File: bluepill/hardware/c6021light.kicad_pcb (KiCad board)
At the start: 2 copper layers, 100 x 50 mm, 82 parts, among them J1 Barrel_Jack_Switch, J10 Conn_01x02, J11 Conn_01x02, J12 XpressNet, J2 Conn_02x04_Odd_Even, J3 Conn_02x16_Row_Letter_First, J30 Loconet, J31 Conn_01x02, J32 Conn_01x02, J4 Conn_01x02, J5 Grove I2C, J50 USB_B_Micro, J51 Conn_01x06, J52 Debug UART, J6 Conn_01x02, J7 Conn_01x02, J8 RJ45, Q30 BC337, Q31 BC547, Q32 BC547, SW1 SW_Push, U1 L7805, U10 SN75176, U2 L7808, U3 MCP2562, U30 LM393, U4 ISO1050DUB, U50 CH340C

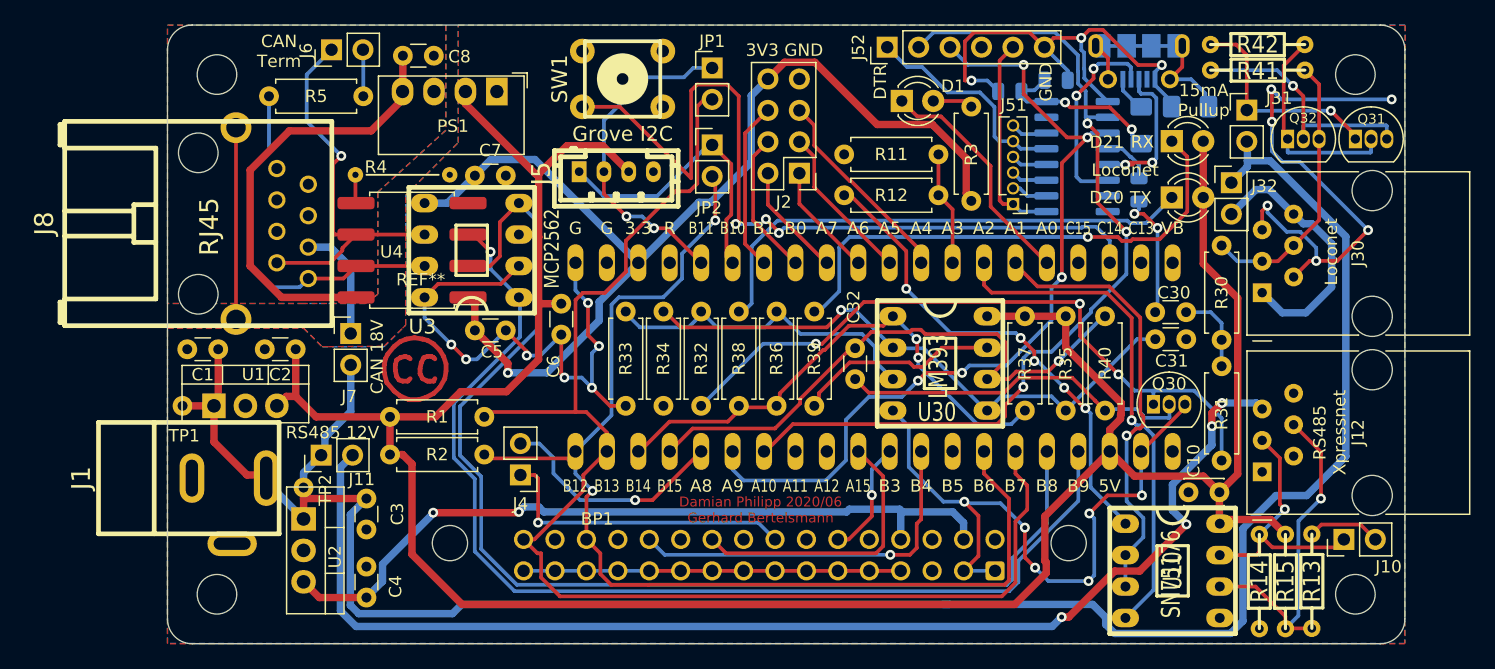
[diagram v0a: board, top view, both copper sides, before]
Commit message: new PCB version 1.1. aka 2020/08 with some small fixes
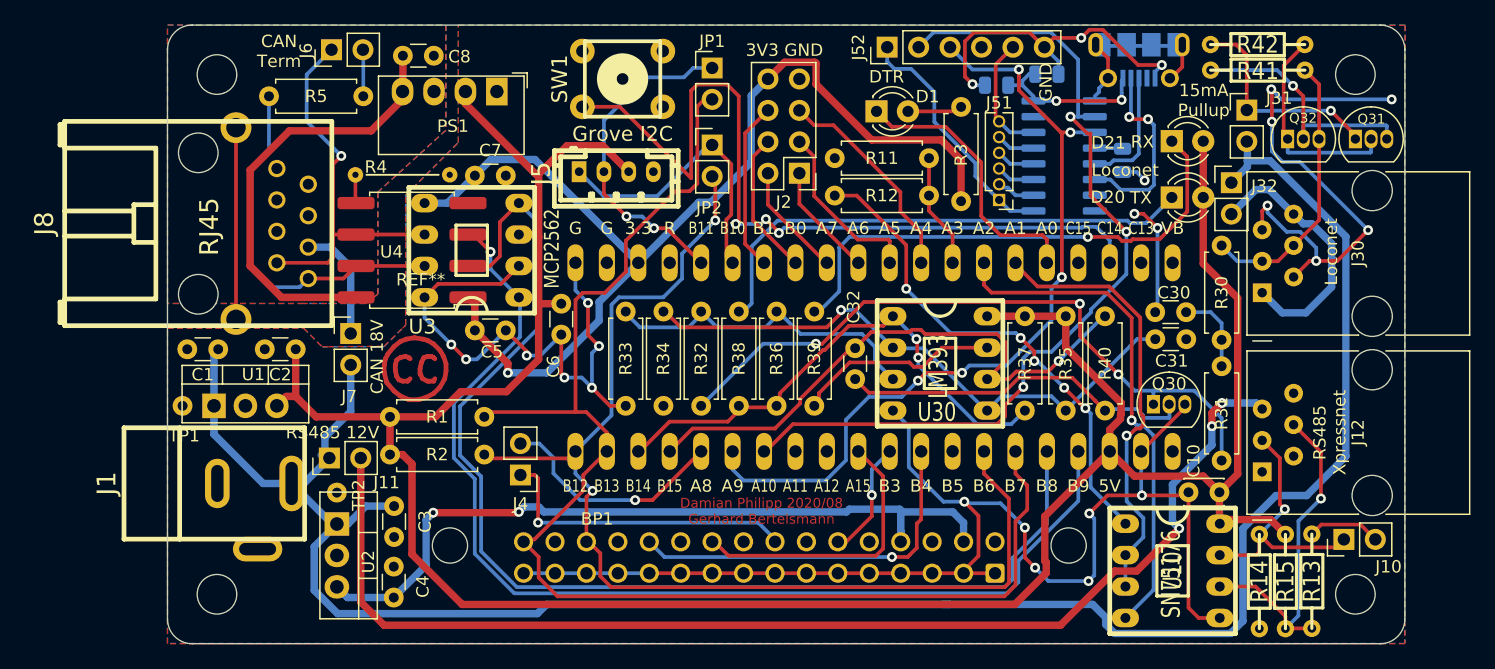
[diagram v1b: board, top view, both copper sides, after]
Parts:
- removed R50, R51: 0, Resistor_SMD:R_1206_3216Metric_Pad1.42x1.75mm_HandSolder
- moved C52 2.73 mm to (177.2, 60.9)
- moved U2 2.72 mm to (113.7, 90.3)
- moved TP2 2.72 mm to (113.7, 87.8)
- moved C3 2.32 mm to (118.3, 88.9)
- moved D1 2.21 mm to (157.3, 57.0)
- moved C4 2.21 mm to (118.3, 96.3)
- moved J1 2.10 mm to (103.8, 87.0)
- moved J51 1.18 mm to (167.2, 64.1)
- moved C51 1.18 mm to (167.0, 54.9)
- moved U50 1.04 mm to (172.5, 60.6)
- moved C50 0.89 mm to (171.1, 54.0)
- moved R3 0.83 mm to (164.1, 64.2)
- moved R11 0.82 mm to (153.9, 60.8)
- moved R12 0.76 mm to (153.9, 63.8)
- moved J11 0.70 mm to (113.1, 85.0)
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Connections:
- J50 pad 1: Net-(J50-Pad1) -> Net-(C50-Pad1)
- J50 pad 6: Net-(J50-Pad6) -> GND
- J51 pad 6: Net-(J51-Pad6) -> /RTS
- J52 pad 1: /DTR -> /CTS
- J52 pad 5: /CTS -> /RTS
- J8 pad 5: GNDD -> Net-(J8-Pad5)
- TP1 pad 1: +12V -> Net-(TP1-Pad1)
- TP2 pad 1: +12V -> Net-(TP2-Pad1)
- U50 pad 14: Net-(J51-Pad6) -> /RTS
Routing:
- net GND: track 223.2 -> 246.5 mm, vias 24 -> 25
- net Net-(J50-Pad6): track 17.1 -> 0.00 mm
- net /DTR: track 17.7 -> 3.15 mm
- net /RTS: track 0.00 -> 10.4 mm
- net Net-(BP1-Pad25): track 19.1 -> 22.5 mm
- net Net-(J11-Pad2): track 100.7 -> 97.3 mm, vias 4 -> 3
- net /CTS: track 17.0 -> 20.0 mm
- net Net-(J51-Pad6): track 3.02 -> 0.00 mm
- net Net-(J50-Pad1): track 2.74 -> 0.00 mm
- net Net-(J50-Pad3): track 12.3 -> 9.92 mm, vias 2 -> 0
- net /TxD: track 68.2 -> 66.0 mm
- net +12V: track 175.0 -> 173.1 mm
- net Net-(C52-Pad1): track 4.16 -> 2.33 mm
- net Net-(BP1-Pad29): track 16.5 -> 18.3 mm
- net Net-(BP1-Pad30): track 12.8 -> 14.3 mm
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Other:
- board text added: "Damian Philipp 2020/08 Gerhard Bertelsmann"
- board text removed: "Damian Philipp 2020/06 Gerhard Bertelsmann"
